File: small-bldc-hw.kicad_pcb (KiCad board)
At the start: 4 copper layers, 65 x 22.4 mm, 98 parts, among them J1 More IO, J2 TEMP, J3 CONN_01X01, J4 CONN_01X01, J5 CONN_01X01, J6 CAN, J7 I2C, J8 CONN_01X01, J9 CONN_01X01, P2 SWD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

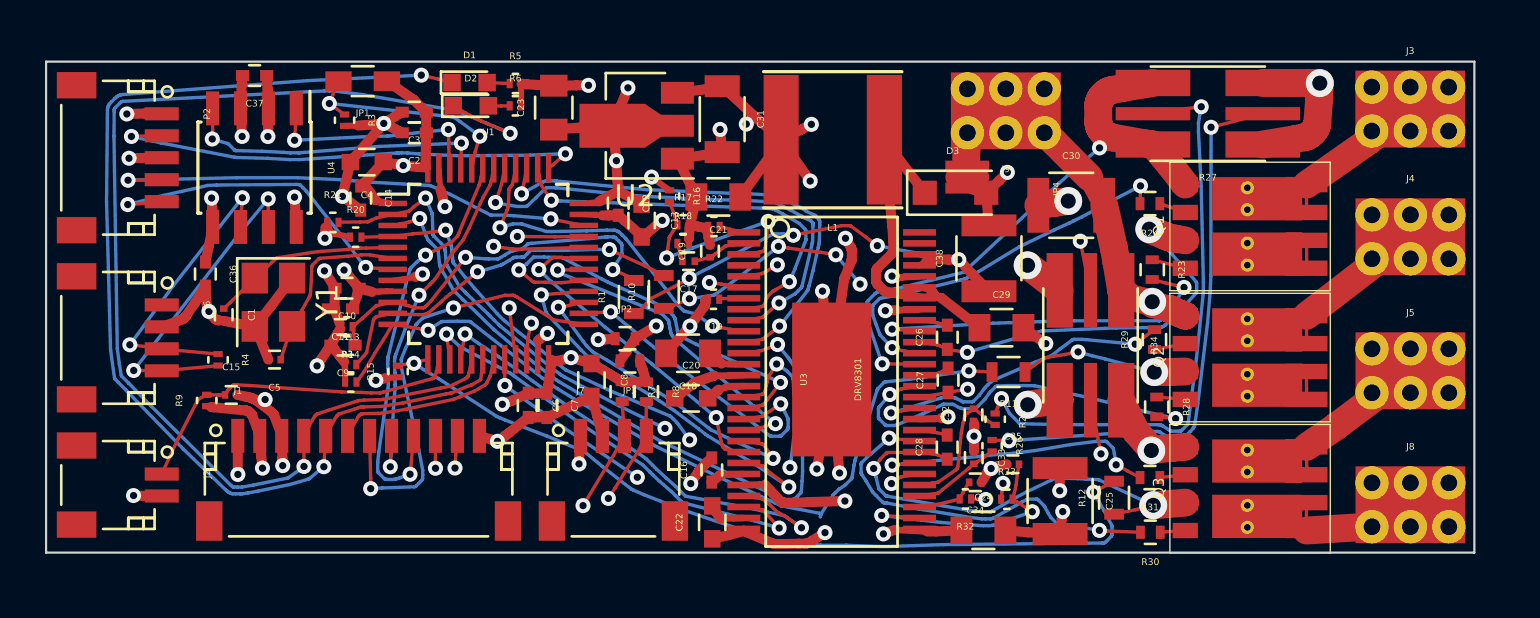
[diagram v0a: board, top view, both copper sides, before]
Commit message: 1 more layer to plane
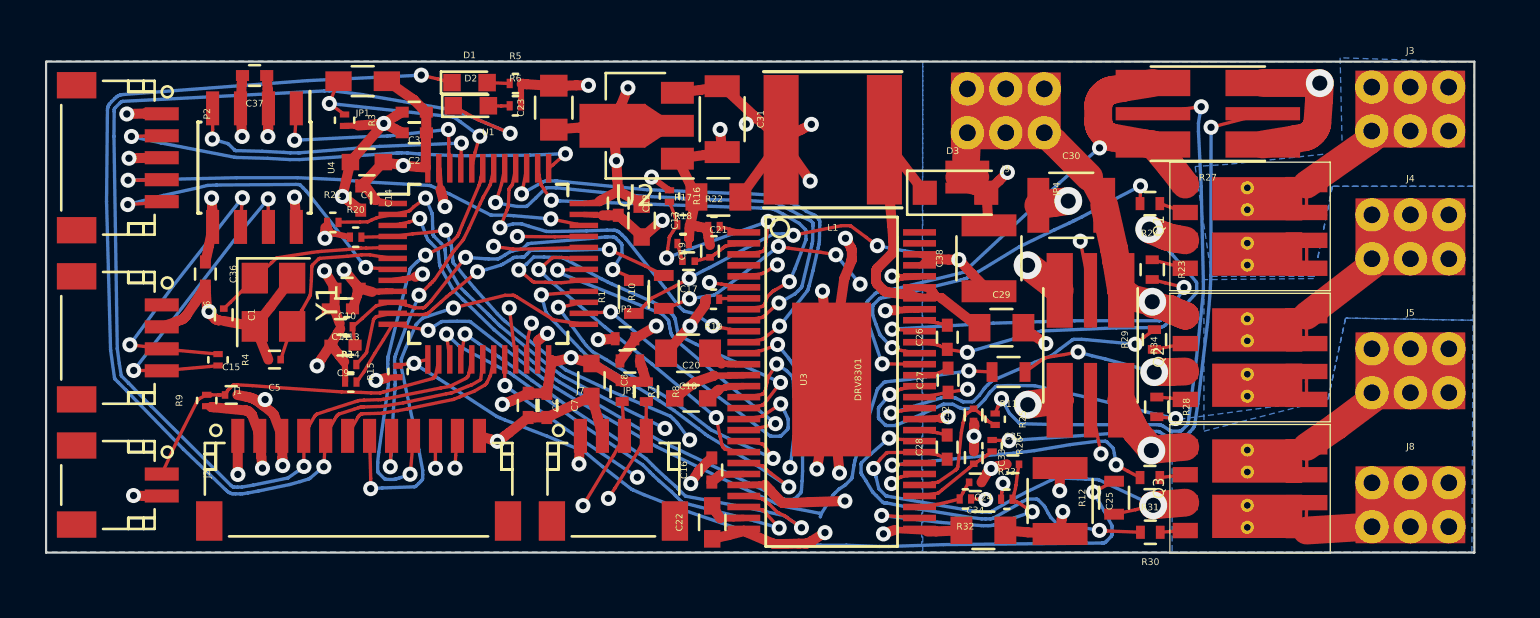
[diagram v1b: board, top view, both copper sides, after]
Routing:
- added copper zone on In1.Cu, net +3V3
- added copper zone on B.Cu, net /power/PHASE_A
- added copper zone on In2.Cu, net /power/PHASE_A
- added copper zone on B.Cu, net /power/PHASE_B
- added copper zone on In2.Cu, net /power/PHASE_B
- added copper zone on B.Cu, net /power/PHASE_C
- added copper zone on In2.Cu, net /power/PHASE_C
- added copper zone on In1.Cu, net DC_SUPPLY
- added copper zone on B.Cu, net GND
- added copper zone on In2.Cu, net GND
- added copper zone on B.Cu, net GNDPWR
- added copper zone on In2.Cu, net GNDPWR
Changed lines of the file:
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@@
 (kicad_pcb (version 4) (host pcbnew 4.0.6)
   (general
-    (links 0)
+    (links 313)
     (no_connects 0)
-    (area 0 0 0 0)
+    (area 118.26896 88.33446 184.962001 113.67752)
     (thickness 1.6)
     (drawings 4)
@@
     (uvia_dia 0.3)
     (uvia_drill 0.1)
+    (add_net +3V3)
+    (add_net +5V)
+    (add_net /ADC_IN9)
+    (add_net /CANH)
+    (add_net /CANL)
+    (add_net /CAN_RX)
+    (add_net /CAN_TX)
+    (add_net /DRV_CS)
+    (add_net /DRV_DC_CAL)
+    (add_net /DRV_EN_GATE)
+    (add_net /DRV_FAULT)
+    (add_net /DRV_OCTW)
+    (add_net /IN_VOLTAGE)
+    (add_net /MISO)
+    (add_net /MOSI)
+    (add_net /NRST)
+    (add_net /PA7)
+    (add_net /PB0)
+    (add_net /PB12)
+    (add_net /PHA_V)
+    (add_net /PHB_V)
+    (add_net /PHC_V)
+    (add_net /SCK)
+    (add_net /SCL)
+    (add_net /SDA)
+    (add_net /SO1)
+    (add_net /SO2)
+    (add_net /SWCLK)
+    (add_net /SWDIO)
+    (add_net /TEMP_MOTOR)
+    (add_net /TIM1_CH1)
+    (add_net /TIM1_CH1N)
+    (add_net /TIM1_CH2)
+    (add_net /TIM1_CH2N)
+    (add_net /TIM1_CH3)
+    (add_net /TIM1_CH3N)
+    (add_net /UART_RX)
+    (add_net /UART_TX)
+    (add_net /USB_DM)
+    (add_net /USB_DP)
+    (add_net /power/GH_A)
+    (add_net /power/GH_B)
+    (add_net /power/GH_C)
+    (add_net /power/GL_A)
+    (add_net /power/GL_B)
+    (add_net /power/GL_C)
+    (add_net /power/PHASE_A)
+    (add_net /power/PHASE_B)
+    (add_net /power/PHASE_C)
+    (add_net /power/SL_A)
+    (add_net /power/SL_C)
+    (add_net /power/SN_A)
+    (add_net /power/SN_C)
+    (add_net /power/SP_A)
+    (add_net /power/SP_C)
+    (add_net DC_SUPPLY)
+    (add_net GND)
+    (add_net GNDPWR)
+    (add_net "Net-(C1-Pad1)")
+    (add_net "Net-(C16-Pad1)")
+    (add_net "Net-(C17-Pad1)")
+    (add_net "Net-(C17-Pad2)")
+    (add_net "Net-(C18-Pad1)")
+    (add_net "Net-(C20-Pad1)")
+    (add_net "Net-(C20-Pad2)")
+    (add_net "Net-(C22-Pad2)")
+    (add_net "Net-(C26-Pad2)")
+    (add_net "Net-(C27-Pad2)")
+    (add_net "Net-(C28-Pad2)")
+    (add_net "Net-(C29-Pad1)")
+    (add_net "Net-(C29-Pad2)")
+    (add_net "Net-(C5-Pad1)")
+    (add_net "Net-(D1-Pad2)")
+    (add_net "Net-(D2-Pad2)")
+    (add_net "Net-(J7-Pad1)")
+    (add_net "Net-(JP1-Pad2)")
+    (add_net "Net-(Q1-Pad2)")
+    (add_net "Net-(Q1-Pad4)")
+    (add_net "Net-(Q2-Pad2)")
+    (add_net "Net-(Q2-Pad4)")
+    (add_net "Net-(Q3-Pad2)")
+    (add_net "Net-(Q3-Pad4)")
+    (add_net "Net-(R16-Pad2)")
+    (add_net "Net-(R19-Pad1)")
+    (add_net "Net-(R22-Pad2)")
+    (add_net "Net-(R25-Pad1)")
+    (add_net "Net-(R26-Pad1)")
+    (add_net "Net-(R32-Pad1)")
+    (add_net "Net-(R33-Pad1)")
   )
   (net_class bigpower ""
@@
   (segment (start 135.932 93.0531) (end 135.569 93.1) (width 0.1524) (layer B.Cu) (net 89))
   (segment (start 138.203 92.812) (end 135.932 93.0531) (width 0.1524) (layer B.Cu) (net 89))
+  (zone (net 2) (net_name GND) (layer In2.Cu) (hatch edge 0.508)
+    (priority 5)
+    (connect_pads yes (clearance 0.508))
+    (min_thickness 0.254)
+    (fill yes (arc_segments 16) (thermal_gap 0.508) (thermal_bridge_width 0.508))
+    (polygon
+      (pts
+        (xy 119.9 89.7) (xy 159.8 89.7) (xy 159.8 95) (xy 164.1 95) (xy 164 108.6)
+        (xy 167.6 108.6) (xy 167.6 112.1) (xy 119.9 112.1)
+      )
+    )
+  )
+  (zone (net 43) (net_name GNDPWR) (layer In2.Cu) (hatch edge 0.508)
+    (priority 11)
+    (connect_pads yes (clearance 0.508))
+    (min_thickness 0.254)
+    (fill yes (arc_segments 16) (thermal_gap 0.508) (thermal_bridge_width 0.508))
+    (polygon
+      (pts
+        (xy 159.8 89.7) (xy 178.5 89.7) (xy 178.5 94.2) (xy 169.8 94.2) (xy 169.8 112)
+        (xy 159.8 112)
+      )
+    )
+  )
+  (zone (net 16) (net_name /power/PHASE_A) (layer In2.Cu) (hatch edge 0.508)
+    (priority 5)
+    (connect_pads yes (clearance 0.508))
+    (min_thickness 0.254)
+    (fill yes (arc_segments 16) (thermal_gap 0.508) (thermal_bridge_width 0.508))
+    (polygon
+      (pts
+        (xy 178.6 89.7) (xy 178.6 94.3) (xy 169.9 94.3) (xy 169.9 100.2) (xy 172.8 100.2)
+        (xy 176.5 100.2) (xy 178.6 99.5) (xy 179.1 95.6) (xy 179.9 95.4) (xy 184.8 95.4)
+        (xy 184.8 89.8)
+      )
+    )
+  )
+  (zone (net 18) (net_name /power/PHASE_B) (layer In2.Cu) (hatch edge 0.508)
+    (priority 4)
+    (connect_pads yes (clearance 0.508))
+    (min_thickness 0.254)
+    (fill yes (arc_segments 16) (thermal_gap 0.508) (thermal_bridge_width 0.508))
+    (polygon
+      (pts
+        (xy 184.9 95.6) (xy 179.2 95.6) (xy 178.4 100.2) (xy 171 100.3) (xy 170.9 102.6)
+        (xy 169.8 102.6) (xy 169.8 106.3) (xy 178.5 106.1) (xy 179 101.5) (xy 184.9 101.5)
+        (xy 184.9 94.8)
+      )
+    )
+  )
+  (zone (net 20) (net_name /power/PHASE_C) (layer In2.Cu) (hatch edge 0.508)
+    (priority 3)
+    (connect_pads yes (clearance 0.508))
+    (min_thickness 0.254)
+    (fill yes (arc_segments 16) (thermal_gap 0.508) (thermal_bridge_width 0.508))
+    (polygon
+      (pts
+        (xy 169.8 106.3) (xy 169.8 112) (xy 179 112) (xy 179 107.6) (xy 184.7 107.6)
+        (xy 184.9 101.5) (xy 179 101.5) (xy 178.4 106.3)
+      )
+    )
+  )
+  (zone (net 15) (net_name DC_SUPPLY) (layer In1.Cu) (hatch edge 0.508)
+    (priority 3)
+    (connect_pads yes (clearance 0.508))
+    (min_thickness 0.254)
+    (fill yes (arc_segments 16) (thermal_gap 0.508) (thermal_bridge_width 0.508))
+    (polygon
+      (pts
+        (xy 184.9 89.7) (xy 168.2 89.7) (xy 168.25 94.7) (xy 161.1 94.95) (xy 161.2 109.45)
+        (xy 161.3 112.15) (xy 170.2 112.1) (xy 184.9 112.1)
+      )
+    )
+  )
+  (zone (net 3) (net_name +3V3) (layer In1.Cu) (hatch edge 0.508)
+    (priority 3)
+    (connect_pads yes (clearance 0.508))
+    (min_thickness 0.254)
+    (fill yes (arc_segments 16) (thermal_gap 0.508) (thermal_bridge_width 0.508))
+    (polygon
+      (pts
+        (xy 119.9 89.7) (xy 159.8 89.7) (xy 159.75 112.1) (xy 119.9 112.1)
+      )
+    )
+  )
+  (zone (net 16) (net_name /power/PHASE_A) (layer B.Cu) (hatch edge 0.508)
+    (priority 15)
+    (connect_pads yes (clearance 0.508))
+    (min_thickness 0.254)
+    (fill yes (arc_segments 16) (thermal_gap 0.508) (thermal_bridge_width 0.508))
+    (polygon
+      (pts
+        (xy 184.9 89.75) (xy 178.8 89.55) (xy 178.9 93.85) (xy 173.7 94.4) (xy 172.2 94.5)
+        (xy 172.95 99.5) (xy 177.6 99.5) (xy 178.45 95.4) (xy 184.9 95.4)
+      )
+    )
+  )
+  (zone (net 18) (net_name /power/PHASE_B) (layer B.Cu) (hatch edge 0.508)
+    (priority 12)
+    (connect_pads yes (clearance 0.508))
+    (min_thickness 0.254)
+    (fill yes (arc_segments 16) (thermal_gap 0.508) (thermal_bridge_width 0.508))
+    (polygon
+      (pts
+        (xy 184.9 95.4) (xy 178.45 95.4) (xy 177.6 99.6) (xy 172.6 99.65) (xy 172.6 106.55)
+        (xy 178.25 105.1) (xy 179.05 101.4) (xy 184.85 101.5) (xy 184.9 95.45)
+      )
+    )
+  )
+  (zone (net 20) (net_name /power/PHASE_C) (layer B.Cu) (hatch edge 0.508)
+    (priority 9)
+    (connect_pads yes (clearance 0.508))
+    (min_thickness 0.254)
+    (fill yes (arc_segments 16) (thermal_gap 0.508) (thermal_bridge_width 0.508))
+    (polygon
+      (pts
+        (xy 171.15 106.05) (xy 171.15 112.05) (xy 184.8 112.05) (xy 184.85 101.5) (xy 179.05 101.4)
+        (xy 178.25 105.1)
+      )
+    )
+  )
+  (zone (net 43) (net_name GNDPWR) (layer B.Cu) (hatch edge 0.508)
+    (priority 1)
+    (connect_pads yes (clearance 0.508))
+    (min_thickness 0.254)
+    (fill yes (arc_segments 16) (thermal_gap 0.508) (thermal_bridge_width 0.508))
+    (polygon
+      (pts
+        (xy 159.8 89.7) (xy 184.9 89.75) (xy 184.9 112.05) (xy 159.8 112.05)
+      )
+    )
+  )
+  (zone (net 2) (net_name GND) (layer B.Cu) (hatch edge 0.508)
+    (priority 8)
+    (connect_pads yes (clearance 0.508))
+    (min_thickness 0.254)
+    (fill yes (arc_segments 16) (thermal_gap 0.508) (thermal_bridge_width 0.508))
+    (polygon
+      (pts
+        (xy 159.8 89.7) (xy 159.75 112.05) (xy 119.9 112.05) (xy 119.9 89.7)
+      )
+    )
+  )
 )

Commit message: all planes done
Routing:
- added copper zone on F.Cu, net /power/PHASE_A
- added copper zone on F.Cu, net /power/PHASE_B
- added copper zone on F.Cu, net /power/PHASE_C
- added copper zone on F.Cu, net DC_SUPPLY
- added copper zone on In2.Cu, net DC_SUPPLY
- added copper zone on F.Cu, net GND
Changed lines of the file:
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@@
   (layers
     (0 F.Cu signal)
-    (1 In1.Cu signal)
-    (2 In2.Cu signal)
-    (31 B.Cu signal)
+    (1 In1.Cu signal hide)
+    (2 In2.Cu signal hide)
+    (31 B.Cu signal hide)
     (35 F.Paste user)
     (36 B.SilkS user)
@@
       (pts
         (xy 178.6 89.7) (xy 178.6 94.3) (xy 169.9 94.3) (xy 169.9 100.2) (xy 172.8 100.2)
-        (xy 176.5 100.2) (xy 178.6 99.5) (xy 179.1 95.6) (xy 179.9 95.4) (xy 184.8 95.4)
+        (xy 176.1 99.15) (xy 177.4 97.55) (xy 179.1 95.6) (xy 179.9 95.4) (xy 184.8 95.4)
         (xy 184.8 89.8)
       )
@@
     (polygon
       (pts
-        (xy 184.9 95.6) (xy 179.2 95.6) (xy 178.4 100.2) (xy 171 100.3) (xy 170.9 102.6)
-        (xy 169.8 102.6) (xy 169.8 106.3) (xy 178.5 106.1) (xy 179 101.5) (xy 184.9 101.5)
+        (xy 184.9 95.6) (xy 179.2 95.6) (xy 176.65 98.05) (xy 171 100.3) (xy 170.9 102.6)
+        (xy 169.8 102.6) (xy 169.8 106.3) (xy 176.65 103.5) (xy 179 101.5) (xy 184.9 101.5)
         (xy 184.9 94.8)
       )
@@
     (polygon
       (pts
-        (xy 169.8 106.3) (xy 169.8 112) (xy 179 112) (xy 179 107.6) (xy 184.7 107.6)
-        (xy 184.9 101.5) (xy 179 101.5) (xy 178.4 106.3)
+        (xy 169.8 106.3) (xy 169.8 112) (xy 173 112) (xy 173.7 109) (xy 184.7 107.6)
+        (xy 184.9 101.5) (xy 179 101.5) (xy 177 103.7)
       )
     )
@@
       )
     )
+  )
+  (zone (net 2) (net_name GND) (layer F.Cu) (hatch edge 0.508)
+    (priority 1)
+    (connect_pads yes (clearance 0.508))
+    (min_thickness 0.254)
+    (fill yes (arc_segments 16) (thermal_gap 0.508) (thermal_bridge_width 0.508))
+    (polygon
+      (pts
+        (xy 159.85 89.7) (xy 119.9 89.7) (xy 119.9 112.1) (xy 159.75 112.1)
+      )
+    )
+  )
+  (zone (net 16) (net_name /power/PHASE_A) (layer F.Cu) (hatch edge 0.508)
+    (priority 5)
+    (connect_pads yes (clearance 0.508))
+    (min_thickness 0.254)
+    (fill yes (arc_segments 16) (thermal_gap 0.508) (thermal_bridge_width 0.508))
+    (polygon
+      (pts
+        (xy 184.95 89.6) (xy 178.65 89.65) (xy 178.6 93.45) (xy 176.2 94.65) (xy 169.05 94.55)
+        (xy 169.25 97.25) (xy 178.05 96.8) (xy 180.8 95.55) (xy 184.9 95.55)
+      )
+    )
+  )
+  (zone (net 18) (net_name /power/PHASE_B) (layer F.Cu) (hatch edge 0.508)
+    (priority 4)
+    (connect_pads yes (clearance 0.508))
+    (min_thickness 0.254)
+    (fill yes (arc_segments 16) (thermal_gap 0.508) (thermal_bridge_width 0.508))
+    (polygon
+      (pts
+        (xy 184.95 95.6) (xy 179.05 95.6) (xy 178.55 97.4) (xy 177.3 100.35) (xy 172.15 100.3)
+        (xy 169.85 100.5) (xy 169.65 104.55) (xy 172.5 104.25) (xy 173.15 103.05) (xy 178.5 103)
+        (xy 180.5 101.85) (xy 184.85 101.9)
+      )
+    )
+  )
+  (zone (net 15) (net_name DC_SUPPLY) (layer In2.Cu) (hatch edge 0.508)
+    (priority 1)
+    (connect_pads yes (clearance 0.508))
+    (min_thickness 0.254)
+    (fill yes (arc_segments 16) (thermal_gap 0.508) (thermal_bridge_width 0.508))
+    (polygon
+      (pts
+        (xy 185 107.9) (xy 173.1 109.05) (xy 173 112.05) (xy 184.9 112.05)
+      )
+    )
+  )
+  (zone (net 20) (net_name /power/PHASE_C) (layer F.Cu) (hatch edge 0.508)
+    (priority 6)
+    (connect_pads yes (clearance 0.508))
+    (min_thickness 0.254)
+    (fill yes (arc_segments 16) (thermal_gap 0.508) (thermal_bridge_width 0.508))
+    (polygon
+      (pts
+        (xy 184.934777 101.5) (xy 179.134777 101.5) (xy 177.334777 106) (xy 169.984777 106.35) (xy 170.55 109.05)
+        (xy 185.9 109.05)
+      )
+    )
+  )
+  (zone (net 15) (net_name DC_SUPPLY) (layer F.Cu) (hatch edge 0.508)
+    (priority 5)
+    (connect_pads yes (clearance 0.508))
+    (min_thickness 0.254)
+    (fill yes (arc_segments 16) (thermal_gap 0.508) (thermal_bridge_width 0.508))
+    (polygon
+      (pts
+        (xy 185.1 112) (xy 172.65 111.85) (xy 172.65 109.1) (xy 185.25 108.55)
+      )
+    )
+  )
+  (zone (net 15) (net_name DC_SUPPLY) (layer F.Cu) (hatch edge 0.508)
+    (priority 1)
+    (connect_pads yes (clearance 0.508))
+    (min_thickness 0.254)
+    (fill yes (arc_segments 16) (thermal_gap 0.508) (thermal_bridge_width 0.508))
+    (polygon
+      (pts
+        (xy 172.65 97.25) (xy 178.5 97.2) (xy 178.95 113) (xy 172.4 113.05)
+      )
+    )

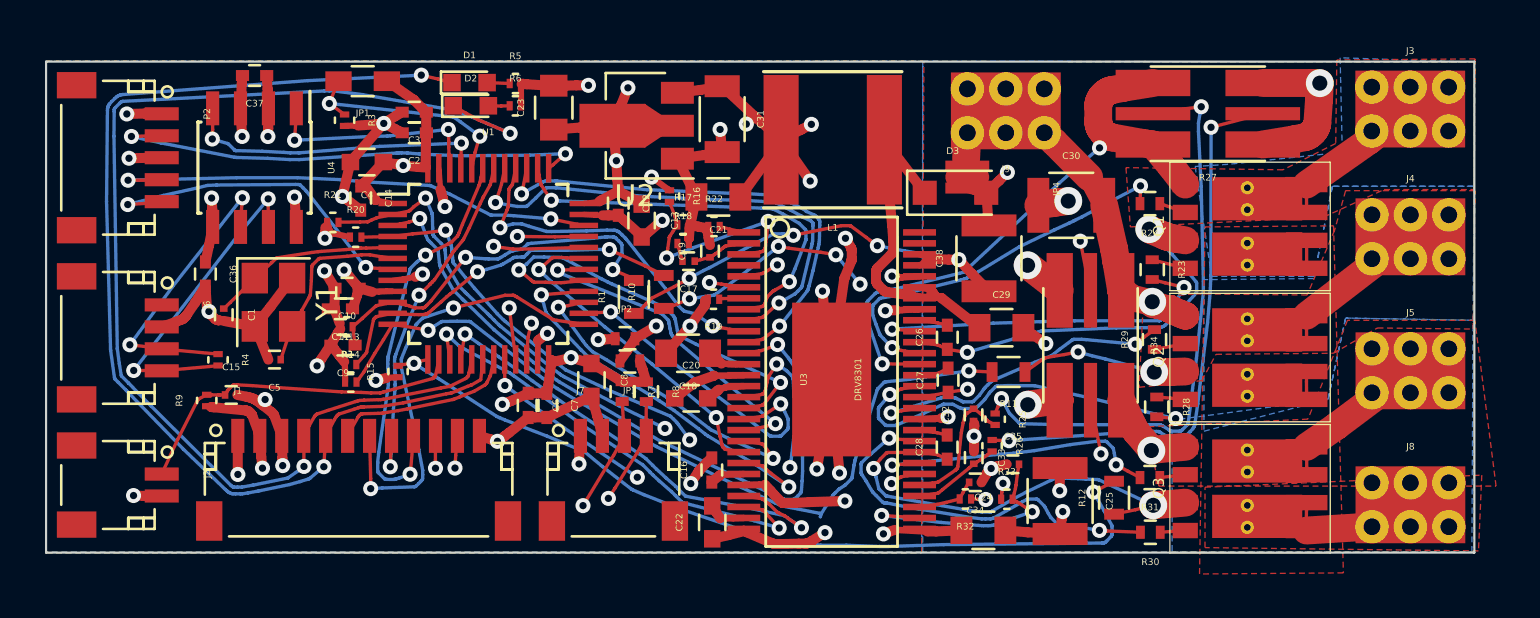
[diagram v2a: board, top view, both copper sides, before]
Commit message: silkscreen references moved
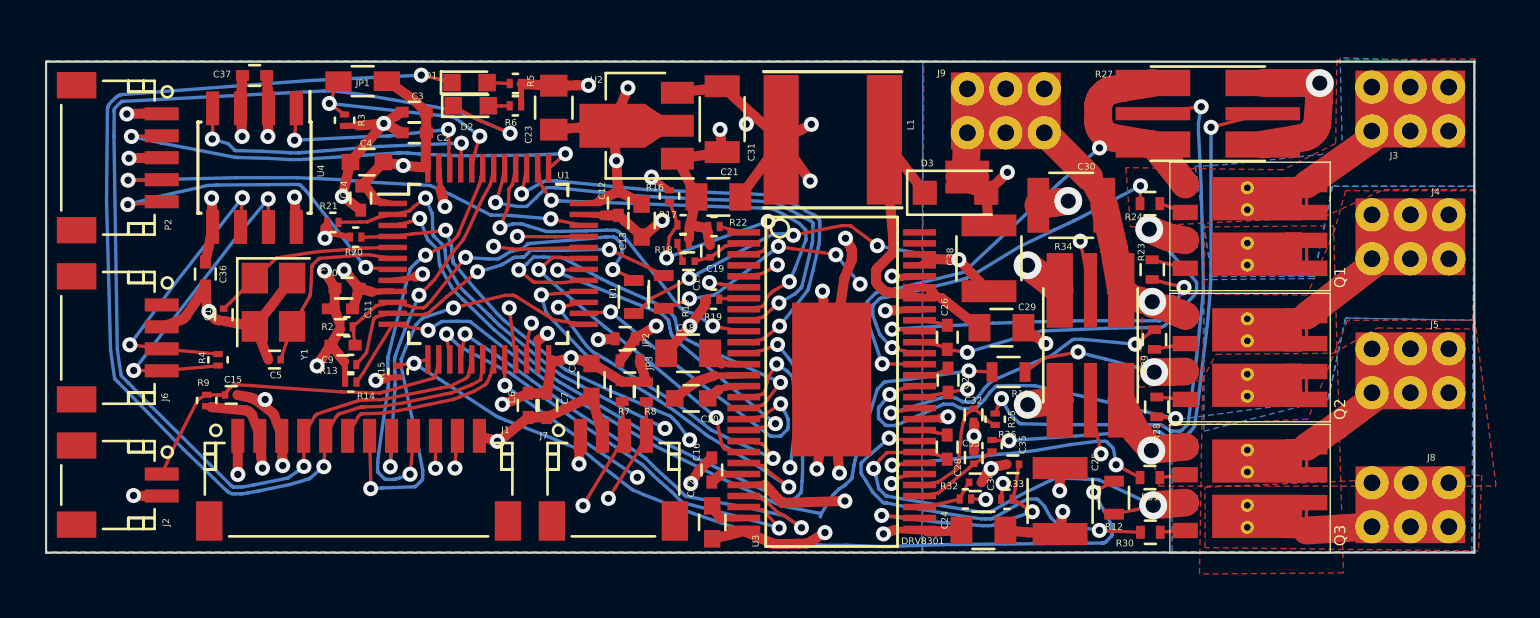
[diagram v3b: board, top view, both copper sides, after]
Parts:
- JP1: footprint Resistors_SMD:R_0603_HandSoldering -> hlib:R_0603_jumper
